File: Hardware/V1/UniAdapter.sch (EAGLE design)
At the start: 19 parts, among them IC1 LD1117S33TR, U1 STM32F072CBT6, X1 CAN Bus

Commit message: UniAdapter 1.0 (PCB-POOL Order)
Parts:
- SB0: device rcl:R-EU_R0603 -> jumper:SJ
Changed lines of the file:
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@@
 </part>
 <part name="GND2" library="supply1" deviceset="GND" device=""/>
-<part name="SB0" library="rcl" deviceset="R-EU_" device="R0603"/>
+<part name="SB0" library="jumper" deviceset="SJ" device=""/>
 <part name="P+4" library="supply1" deviceset="VCC" device=""/>
 </parts>
@@
 </instance>
 <instance part="GND2" gate="1" x="111.76" y="20.32" rot="R90"/>
-<instance part="SB0" gate="G$1" x="93.98" y="10.16"/>
+<instance part="SB0" gate="1" x="93.98" y="10.16"/>
 <instance part="P+4" gate="VCC" x="114.3" y="10.16" rot="R270"/>
 </instances>
@@
 </segment>
 <segment>
-<pinref part="SB0" gate="G$1" pin="2"/>
+<pinref part="SB0" gate="1" pin="2"/>
 <wire x1="111.76" y1="10.16" x2="99.06" y2="10.16" width="0.1524" layer="91"/>
 <pinref part="P+4" gate="VCC" pin="VCC"/>
@@
 <wire x1="88.9" y1="20.32" x2="81.28" y2="20.32" width="0.1524" layer="91"/>
 <label x="71.12" y="20.32" size="1.778" layer="95"/>
-<pinref part="SB0" gate="G$1" pin="1"/>
+<pinref part="SB0" gate="1" pin="1"/>
 <wire x1="81.28" y1="20.32" x2="71.12" y2="20.32" width="0.1524" layer="91"/>
 <wire x1="88.9" y1="10.16" x2="81.28" y2="10.16" width="0.1524" layer="91"/>

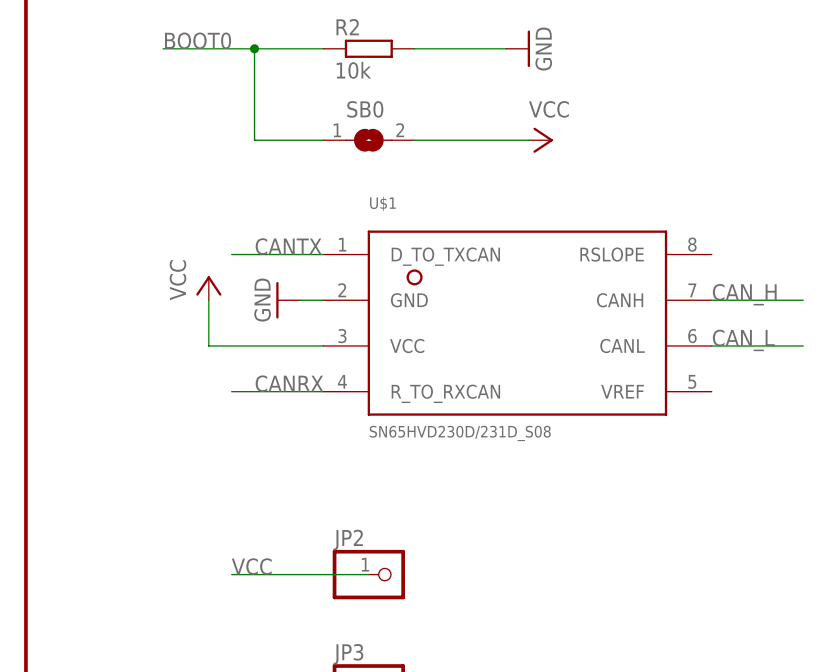
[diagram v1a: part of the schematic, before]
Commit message: Replace HVD230 <-> HVD232
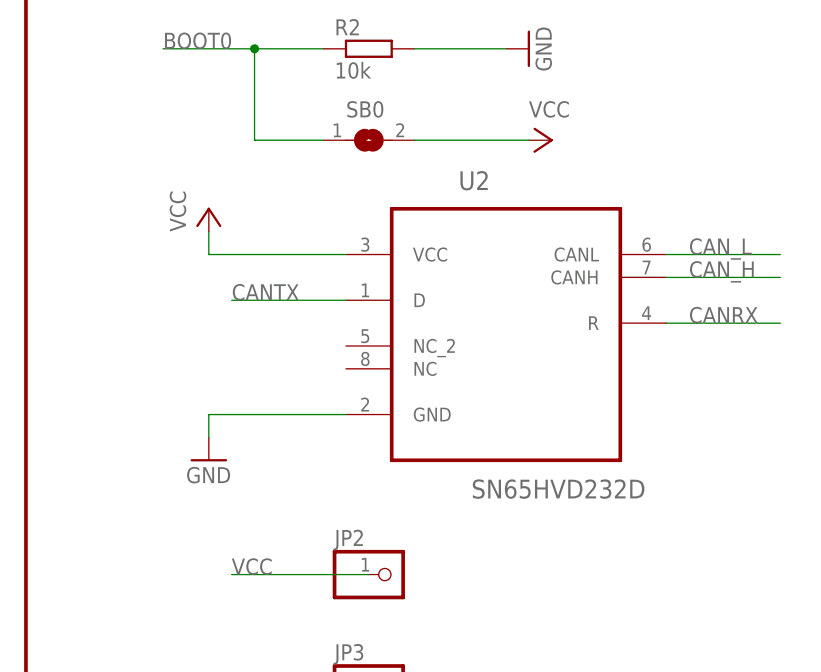
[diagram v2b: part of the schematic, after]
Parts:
- removed U$1: SN65HVD230D/231D_S08, can:SN65HVD230D/231D_S08
- added U2: SN65HVD232D, texas:SN65HVD232D
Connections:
- net CANRX: now also U2.R; no longer U$1.R_TO_RXCAN
- net CANTX: now also U2.D; no longer U$1.D_TO_TXCAN
- net CAN_H: now also U2.CANH; no longer U$1.CANH
- net CAN_L: now also U2.CANL; no longer U$1.CANL
- net GND: now also U2.GND; no longer U$1.GND
- net VCC: now also U2.VCC; no longer U$1.VCC
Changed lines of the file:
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@@
 <grid distance="0.1" unitdist="inch" unit="inch" style="lines" multiple="1" display="no" altdistance="0.01" altunitdist="inch" altunit="inch"/>
 <layers>
-<layer number="1" name="Top" color="4" fill="1" visible="yes" active="no"/>
-<layer number="16" name="Bottom" color="1" fill="1" visible="yes" active="no"/>
-<layer number="17" name="Pads" color="2" fill="1" visible="yes" active="no"/>
-<layer number="18" name="Vias" color="2" fill="1" visible="yes" active="no"/>
-<layer number="19" name="Unrouted" color="14" fill="1" visible="yes" active="no"/>
-<layer number="20" name="Dimension" color="15" fill="1" visible="yes" active="no"/>
-<layer number="21" name="tPlace" color="7" fill="1" visible="yes" active="no"/>
-<layer number="22" name="bPlace" color="7" fill="1" visible="yes" active="no"/>
-<layer number="23" name="tOrigins" color="15" fill="1" visible="yes" active="no"/>
-<layer number="24" name="bOrigins" color="15" fill="1" visible="yes" active="no"/>
-<layer number="25" name="tNames" color="7" fill="1" visible="yes" active="no"/>
-<layer number="26" name="bNames" color="7" fill="1" visible="yes" active="no"/>
-<layer number="27" name="tValues" color="7" fill="1" visible="yes" active="no"/>
-<layer number="28" name="bValues" color="7" fill="1" visible="yes" active="no"/>
+<layer number="1" name="Top" color="4" fill="1" visible="no" active="no"/>
+<layer number="16" name="Bottom" color="1" fill="1" visible="no" active="no"/>
+<layer number="17" name="Pads" color="2" fill="1" visible="no" active="no"/>
+<layer number="18" name="Vias" color="2" fill="1" visible="no" active="no"/>
+<layer number="19" name="Unrouted" color="14" fill="1" visible="no" active="no"/>
+<layer number="20" name="Dimension" color="15" fill="1" visible="no" active="no"/>
+<layer number="21" name="tPlace" color="7" fill="1" visible="no" active="no"/>
+<layer number="22" name="bPlace" color="7" fill="1" visible="no" active="no"/>
+<layer number="23" name="tOrigins" color="15" fill="1" visible="no" active="no"/>
+<layer number="24" name="bOrigins" color="15" fill="1" visible="no" active="no"/>
+<layer number="25" name="tNames" color="7" fill="1" visible="no" active="no"/>
+<layer number="26" name="bNames" color="7" fill="1" visible="no" active="no"/>
+<layer number="27" name="tValues" color="7" fill="1" visible="no" active="no"/>
+<layer number="28" name="bValues" color="7" fill="1" visible="no" active="no"/>
 <layer number="29" name="tStop" color="7" fill="3" visible="no" active="no"/>
 <layer number="30" name="bStop" color="7" fill="6" visible="no" active="no"/>
@@
 <layer number="35" name="tGlue" color="7" fill="4" visible="no" active="no"/>
 <layer number="36" name="bGlue" color="7" fill="5" visible="no" active="no"/>
-<layer number="37" name="tTest" color="7" fill="1" visible="yes" active="no"/>
-<layer number="38" name="bTest" color="7" fill="1" visible="yes" active="no"/>
+<layer number="37" name="tTest" color="7" fill="1" visible="no" active="no"/>
+<layer number="38" name="bTest" color="7" fill="1" visible="no" active="no"/>
 <layer number="39" name="tKeepout" color="4" fill="11" visible="no" active="no"/>
 <layer number="40" name="bKeepout" color="1" fill="11" visible="no" active="no"/>
@@
 <layer number="44" name="Drills" color="7" fill="1" visible="no" active="no"/>
 <layer number="45" name="Holes" color="7" fill="1" visible="no" active="no"/>
-<layer number="46" name="Milling" color="3" fill="1" visible="yes" active="no"/>
-<layer number="47" name="Measures" color="7" fill="1" visible="yes" active="no"/>
-<layer number="48" name="Document" color="7" fill="1" visible="yes" active="no"/>
-<layer number="49" name="Reference" color="7" fill="1" visible="yes" active="no"/>
-<layer number="50" name="dxf" color="7" fill="1" visible="yes" active="no"/>
-<layer number="51" name="tDocu" color="7" fill="1" visible="yes" active="no"/>
-<layer number="52" name="bDocu" color="7" fill="1" visible="yes" active="no"/>
-<layer number="53" name="tGND_GNDA" color="7" fill="9" visible="yes" active="no"/>
-<layer number="54" name="bGND_GNDA" color="1" fill="9" visible="yes" active="no"/>
-<layer number="56" name="wert" color="7" fill="1" visible="yes" active="no"/>
+<layer number="46" name="Milling" color="3" fill="1" visible="no" active="no"/>
+<layer number="47" name="Measures" color="7" fill="1" visible="no" active="no"/>
+<layer number="48" name="Document" color="7" fill="1" visible="no" active="no"/>
+<layer number="49" name="Reference" color="7" fill="1" visible="no" active="no"/>
+<layer number="50" name="dxf" color="7" fill="1" visible="no" active="no"/>
+<layer number="51" name="tDocu" color="7" fill="1" visible="no" active="no"/>
+<layer number="52" name="bDocu" color="7" fill="1" visible="no" active="no"/>
+<layer number="53" name="tGND_GNDA" color="7" fill="9" visible="no" active="no"/>
+<layer number="54" name="bGND_GNDA" color="1" fill="9" visible="no" active="no"/>
+<layer number="56" name="wert" color="7" fill="1" visible="no" active="no"/>
 <layer number="90" name="Modules" color="5" fill="1" visible="yes" active="yes"/>
 <layer number="91" name="Nets" color="2" fill="1" visible="yes" active="yes"/>
@@
 </part>
 <part name="GND4" library="supply1" deviceset="GND" device=""/>
-<part name="U$1" library="can" deviceset="SN65HVD230D/231D_" device="S08"/>
 <part name="R1" library="rcl" deviceset="R-EU_" device="R0603" value="120 Ohm">
 <attribute name="OC_FARNELL" value="2331714"/>
@@
 <part name="SB0" library="jumper" deviceset="SJ" device=""/>
 <part name="P+4" library="supply1" deviceset="VCC" device=""/>
+<part name="U2" library="texas" deviceset="SN65HVD232D" device=""/>
 </parts>
 <sheets>
@@
 </instance>
 <instance part="GND4" gate="1" x="71.12" y="58.42"/>
-<instance part="U$1" gate="G$1" x="101.6" y="-10.16"/>
 <instance part="R1" gate="G$1" x="2.54" y="66.04">
 <attribute name="OC_FARNELL" x="2.54" y="66.04" size="1.778" layer="96" display="off"/>
 </instance>
-<instance part="GND3" gate="1" x="83.82" y="-7.62" rot="R270"/>
-<instance part="VCC" gate="VCC" x="76.2" y="-5.08"/>
+<instance part="GND3" gate="1" x="76.2" y="-25.4"/>
+<instance part="VCC" gate="VCC" x="76.2" y="2.54"/>
 <instance part="U1" gate="A" x="33.02" y="-2.54"/>
 <instance part="IC1" gate="G$1" x="45.72" y="78.74"/>
@@
 <instance part="SB0" gate="1" x="93.98" y="10.16"/>
 <instance part="P+4" gate="VCC" x="114.3" y="10.16" rot="R270"/>
+<instance part="U2" gate="A" x="109.22" y="-7.62"/>
 </instances>
 <busses>
@@
 </segment>
 <segment>
-<pinref part="U$1" gate="G$1" pin="VCC"/>
-<wire x1="88.9" y1="-12.7" x2="76.2" y2="-12.7" width="0.1524" layer="91"/>
+<wire x1="91.44" y1="-2.54" x2="76.2" y2="-2.54" width="0.1524" layer="91"/>
 <pinref part="VCC" gate="VCC" pin="VCC"/>
-<wire x1="76.2" y1="-12.7" x2="76.2" y2="-7.62" width="0.1524" layer="91"/>
+<wire x1="76.2" y1="-2.54" x2="76.2" y2="0" width="0.1524" layer="91"/>
+<pinref part="U2" gate="A" pin="VCC"/>
 </segment>
 <segment>
@@
 <net name="CANRX" class="0">
 <segment>
-<pinref part="U$1" gate="G$1" pin="R_TO_RXCAN"/>
-<wire x1="88.9" y1="-17.78" x2="78.74" y2="-17.78" width="0.1524" layer="91"/>
-<label x="81.28" y="-17.78" size="1.778" layer="95"/>
+<wire x1="139.7" y1="-10.16" x2="127" y2="-10.16" width="0.1524" layer="91"/>
+<label x="129.54" y="-10.16" size="1.778" layer="95"/>
+<pinref part="U2" gate="A" pin="R"/>
 </segment>
 <segment>
@@
 <net name="CANTX" class="0">
 <segment>
-<pinref part="U$1" gate="G$1" pin="D_TO_TXCAN"/>
-<wire x1="88.9" y1="-2.54" x2="78.74" y2="-2.54" width="0.1524" layer="91"/>
-<label x="81.28" y="-2.54" size="1.778" layer="95"/>
+<wire x1="91.44" y1="-7.62" x2="78.74" y2="-7.62" width="0.1524" layer="91"/>
+<label x="78.74" y="-7.62" size="1.778" layer="95"/>
+<pinref part="U2" gate="A" pin="D"/>
 </segment>
 <segment>
@@
 </segment>
 <segment>
-<pinref part="U$1" gate="G$1" pin="CANL"/>
-<wire x1="132.08" y1="-12.7" x2="142.24" y2="-12.7" width="0.1524" layer="91"/>
-<label x="132.08" y="-12.7" size="1.778" layer="95"/>
+<wire x1="127" y1="-2.54" x2="139.7" y2="-2.54" width="0.1524" layer="91"/>
+<label x="129.54" y="-2.54" size="1.778" layer="95"/>
+<pinref part="U2" gate="A" pin="CANL"/>
 </segment>
 </net>
@@
 </segment>
 <segment>
-<pinref part="U$1" gate="G$1" pin="CANH"/>
-<wire x1="132.08" y1="-7.62" x2="142.24" y2="-7.62" width="0.1524" layer="91"/>
-<label x="132.08" y="-7.62" size="1.778" layer="95"/>
+<wire x1="127" y1="-5.08" x2="139.7" y2="-5.08" width="0.1524" layer="91"/>
+<label x="129.54" y="-5.08" size="1.778" layer="95"/>
+<pinref part="U2" gate="A" pin="CANH"/>
 </segment>
 </net>
@@
 <wire x1="45.72" y1="66.04" x2="45.72" y2="63.5" width="0.1524" layer="91"/>
 <junction x="45.72" y="63.5"/>
-</segment>
-<segment>
-<pinref part="U$1" gate="G$1" pin="GND"/>
-<wire x1="88.9" y1="-7.62" x2="86.36" y2="-7.62" width="0.1524" layer="91"/>
-<pinref part="GND3" gate="1" pin="GND"/>
 </segment>
 <segment>
@@
 <label x="78.74" y="-50.8" size="1.778" layer="95"/>
 </segment>
-</net>
+<segment>
+<pinref part="U2" gate="A" pin="GND"/>
+<pinref part="GND3" gate="1" pin="GND"/>
+<wire x1="91.44" y1="-20.32" x2="76.2" y2="-20.32" width="0.1524" layer="91"/>
+<wire x1="76.2" y1="-20.32" x2="76.2" y2="-22.86" width="0.1524" layer="91"/>
+</segment>
+</net>

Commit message: [HW] UniAdapter 1.1
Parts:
- removed JP1: (no value), pinhead:PINHD-1X8
- removed JP2, JP3: (no value), pinhead:PINHD-1X1
- removed SB0: (no value), jumper:SJ
- added EXTENS.: SM05B-SRSS-TB, con-jst2:SM05B-SRSS-TB
- added LED_GREEN, LED_RED: (no value), led:LEDCHIPLED_0603
- added PORT1, PORT2: SM03B-SRSS-TB, con-jst2:SM03B-SRSS-TB
- added R3: 1.8K, rcl:R-EU_R0603
- added R4, R5: 55Ohm, rcl:R-EU_R0603
- added X2: CAN Bus, con-molex-micro-fit-3_0:HEADER_POS4_43650-0412
- C2: OC_FARNELL 1658246RL -> 1432447
- C4: value 10nF -> 100nF; OC_FARNELL 1759022 -> 1759016
- C6: value 100nF -> 10nF; OC_FARNELL 1759016 -> 1759022
- R1: value 120 Ohm -> 10k; OC_FARNELL 2331714 -> 2331740
- R2: value 10k -> 1.8K; OC_FARNELL 2331740RL -> 2331730
- renumbered U1 to IC3, U2 to IC2
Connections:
- removed net NC1: JP1.3
- removed net NC2: JP1.7
- new net I2C1_SCL: EXTENS.-2.S, IC3.PB8, R2.2
- new net I2C1_SDA: EXTENS.-1.S, IC3.PB9, R3.2
- new net LD_GREEN: IC3.PA1, R5.1
- new net LD_RED: IC3.PA0-WKUP, R4.1
- new net N$3: LED_RED.A, R4.2
- new net N$4: LED_GREEN.A, R5.2
- net 6V: now also X2.4
- net BOOT0: now also EXTENS.-3.S, R1.1; no longer R2.1, SB0.1
- net CAN_H: now also X2.2; no longer R1.2
- net CAN_L: now also X2.1; no longer R1.1
- net GND: now also EXTENS.-5.S, LED_GREEN.C, LED_RED.C, PORT1-3.S, PORT2-3.S, R1.2, X2.3; no longer JP1.4, JP1.8, JP3.1, R2.2
- net USART1RX: now also PORT1-2.S; no longer JP1.1
- net USART1TX: now also PORT1-1.S; no longer JP1.2
- net USART2RX: now also PORT2-2.S; no longer JP1.5
- net USART2TX: now also PORT2-1.S; no longer JP1.6
- net VCC: now also EXTENS.-4.S, R2.1, R3.1; no longer JP2.1, SB0.2
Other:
- moved on the sheet: C1, C2, C4, C6, IC1, R1, R2, X1

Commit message: Leds added
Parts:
- LD1: value (none) -> RED
- LD2: value (none) -> GREEN
- renumbered LED_GREEN to LD2, LED_RED to LD1
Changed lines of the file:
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@@
 <grid distance="0.1" unitdist="inch" unit="inch" style="lines" multiple="1" display="no" altdistance="0.01" altunitdist="inch" altunit="inch"/>
 <layers>
-<layer number="1" name="Top" color="4" fill="1" visible="yes" active="no"/>
-<layer number="16" name="Bottom" color="1" fill="1" visible="yes" active="no"/>
-<layer number="17" name="Pads" color="2" fill="1" visible="yes" active="no"/>
-<layer number="18" name="Vias" color="2" fill="1" visible="yes" active="no"/>
-<layer number="19" name="Unrouted" color="14" fill="1" visible="yes" active="no"/>
-<layer number="20" name="Dimension" color="15" fill="1" visible="yes" active="no"/>
-<layer number="21" name="tPlace" color="7" fill="1" visible="yes" active="no"/>
-<layer number="22" name="bPlace" color="7" fill="1" visible="yes" active="no"/>
-<layer number="23" name="tOrigins" color="15" fill="1" visible="yes" active="no"/>
-<layer number="24" name="bOrigins" color="15" fill="1" visible="yes" active="no"/>
-<layer number="25" name="tNames" color="7" fill="1" visible="yes" active="no"/>
-<layer number="26" name="bNames" color="7" fill="1" visible="yes" active="no"/>
-<layer number="27" name="tValues" color="7" fill="1" visible="yes" active="no"/>
-<layer number="28" name="bValues" color="7" fill="1" visible="yes" active="no"/>
+<layer number="1" name="Top" color="4" fill="1" visible="no" active="no"/>
+<layer number="16" name="Bottom" color="1" fill="1" visible="no" active="no"/>
+<layer number="17" name="Pads" color="2" fill="1" visible="no" active="no"/>
+<layer number="18" name="Vias" color="2" fill="1" visible="no" active="no"/>
+<layer number="19" name="Unrouted" color="14" fill="1" visible="no" active="no"/>
+<layer number="20" name="Dimension" color="15" fill="1" visible="no" active="no"/>
+<layer number="21" name="tPlace" color="7" fill="1" visible="no" active="no"/>
+<layer number="22" name="bPlace" color="7" fill="1" visible="no" active="no"/>
+<layer number="23" name="tOrigins" color="15" fill="1" visible="no" active="no"/>
+<layer number="24" name="bOrigins" color="15" fill="1" visible="no" active="no"/>
+<layer number="25" name="tNames" color="7" fill="1" visible="no" active="no"/>
+<layer number="26" name="bNames" color="7" fill="1" visible="no" active="no"/>
+<layer number="27" name="tValues" color="7" fill="1" visible="no" active="no"/>
+<layer number="28" name="bValues" color="7" fill="1" visible="no" active="no"/>
 <layer number="29" name="tStop" color="7" fill="3" visible="no" active="no"/>
 <layer number="30" name="bStop" color="7" fill="6" visible="no" active="no"/>
@@
 <layer number="35" name="tGlue" color="7" fill="4" visible="no" active="no"/>
 <layer number="36" name="bGlue" color="7" fill="5" visible="no" active="no"/>
-<layer number="37" name="tTest" color="7" fill="1" visible="yes" active="no"/>
-<layer number="38" name="bTest" color="7" fill="1" visible="yes" active="no"/>
+<layer number="37" name="tTest" color="7" fill="1" visible="no" active="no"/>
+<layer number="38" name="bTest" color="7" fill="1" visible="no" active="no"/>
 <layer number="39" name="tKeepout" color="4" fill="11" visible="no" active="no"/>
 <layer number="40" name="bKeepout" color="1" fill="11" visible="no" active="no"/>
@@
 <layer number="44" name="Drills" color="7" fill="1" visible="no" active="no"/>
 <layer number="45" name="Holes" color="7" fill="1" visible="no" active="no"/>
-<layer number="46" name="Milling" color="3" fill="1" visible="yes" active="no"/>
-<layer number="47" name="Measures" color="7" fill="1" visible="yes" active="no"/>
-<layer number="48" name="Document" color="7" fill="1" visible="yes" active="no"/>
-<layer number="49" name="Reference" color="7" fill="1" visible="yes" active="no"/>
-<layer number="50" name="dxf" color="7" fill="1" visible="yes" active="no"/>
-<layer number="51" name="tDocu" color="7" fill="1" visible="yes" active="no"/>
-<layer number="52" name="bDocu" color="7" fill="1" visible="yes" active="no"/>
-<layer number="53" name="tGND_GNDA" color="7" fill="9" visible="yes" active="no"/>
-<layer number="54" name="bGND_GNDA" color="1" fill="9" visible="yes" active="no"/>
-<layer number="56" name="wert" color="7" fill="1" visible="yes" active="no"/>
+<layer number="46" name="Milling" color="3" fill="1" visible="no" active="no"/>
+<layer number="47" name="Measures" color="7" fill="1" visible="no" active="no"/>
+<layer number="48" name="Document" color="7" fill="1" visible="no" active="no"/>
+<layer number="49" name="Reference" color="7" fill="1" visible="no" active="no"/>
+<layer number="50" name="dxf" color="7" fill="1" visible="no" active="no"/>
+<layer number="51" name="tDocu" color="7" fill="1" visible="no" active="no"/>
+<layer number="52" name="bDocu" color="7" fill="1" visible="no" active="no"/>
+<layer number="53" name="tGND_GNDA" color="7" fill="9" visible="no" active="no"/>
+<layer number="54" name="bGND_GNDA" color="1" fill="9" visible="no" active="no"/>
+<layer number="56" name="wert" color="7" fill="1" visible="no" active="no"/>
 <layer number="90" name="Modules" color="5" fill="1" visible="yes" active="yes"/>
 <layer number="91" name="Nets" color="2" fill="1" visible="yes" active="yes"/>
@@
 <part name="R4" library="rcl" deviceset="R-EU_" device="R0603" value="55Ohm"/>
 <part name="R5" library="rcl" deviceset="R-EU_" device="R0603" value="55Ohm"/>
-<part name="LED_RED" library="led" deviceset="LED" device="CHIPLED_0603"/>
-<part name="LED_GREEN" library="led" deviceset="LED" device="CHIPLED_0603"/>
+<part name="LD1" library="led" deviceset="LED" device="CHIPLED_0603" value="RED"/>
+<part name="LD2" library="led" deviceset="LED" device="CHIPLED_0603" value="GREEN"/>
 <part name="GND5" library="supply1" deviceset="GND" device=""/>
 </parts>
@@
 <instance part="R4" gate="G$1" x="111.76" y="30.48"/>
 <instance part="R5" gate="G$1" x="111.76" y="20.32"/>
-<instance part="LED_RED" gate="G$1" x="127" y="30.48" rot="R90"/>
-<instance part="LED_GREEN" gate="G$1" x="127" y="20.32" rot="R90"/>
+<instance part="LD1" gate="G$1" x="127" y="30.48" rot="R90"/>
+<instance part="LD2" gate="G$1" x="127" y="20.32" rot="R90"/>
 <instance part="GND5" gate="1" x="134.62" y="15.24"/>
 </instances>
@@
 </segment>
 <segment>
-<pinref part="LED_GREEN" gate="G$1" pin="C"/>
+<pinref part="LD2" gate="G$1" pin="C"/>
 <pinref part="GND5" gate="1" pin="GND"/>
 <wire x1="132.08" y1="20.32" x2="134.62" y2="20.32" width="0.1524" layer="91"/>
-<pinref part="LED_RED" gate="G$1" pin="C"/>
+<pinref part="LD1" gate="G$1" pin="C"/>
 <wire x1="134.62" y1="20.32" x2="134.62" y2="17.78" width="0.1524" layer="91"/>
 <wire x1="132.08" y1="30.48" x2="134.62" y2="30.48" width="0.1524" layer="91"/>
@@
 <segment>
 <pinref part="R4" gate="G$1" pin="2"/>
-<pinref part="LED_RED" gate="G$1" pin="A"/>
+<pinref part="LD1" gate="G$1" pin="A"/>
 <wire x1="116.84" y1="30.48" x2="124.46" y2="30.48" width="0.1524" layer="91"/>
 </segment>
@@
 <net name="N$4" class="0">
 <segment>
-<pinref part="LED_GREEN" gate="G$1" pin="A"/>
+<pinref part="LD2" gate="G$1" pin="A"/>
 <pinref part="R5" gate="G$1" pin="2"/>
 <wire x1="124.46" y1="20.32" x2="116.84" y2="20.32" width="0.1524" layer="91"/>
